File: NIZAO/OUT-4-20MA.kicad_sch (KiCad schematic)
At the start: 11 parts, among them Q1 NCE60P04R, U16 GP8302-TC50-EW

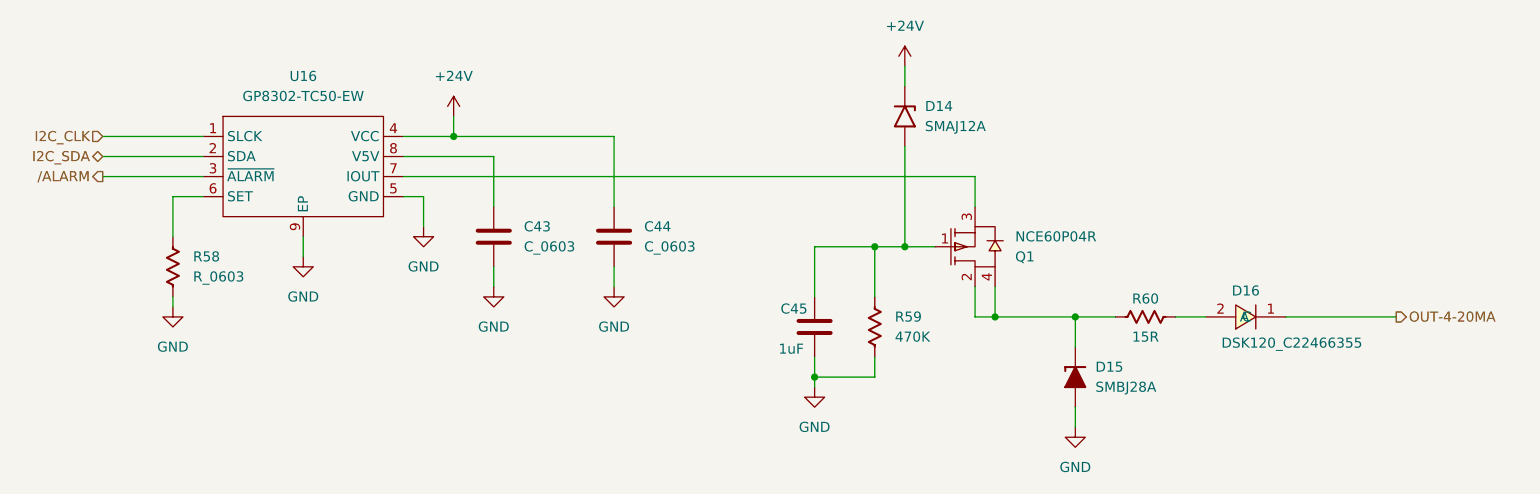
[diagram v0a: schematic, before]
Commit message: Colocandos los 3d de los componetes en la placa NIZAO
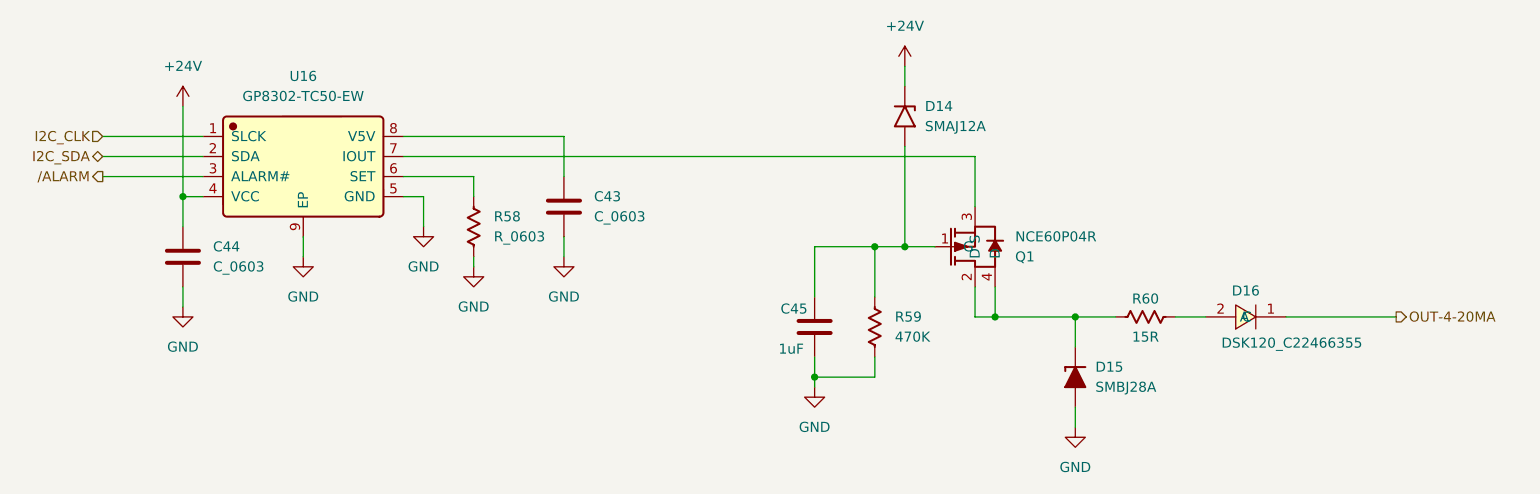
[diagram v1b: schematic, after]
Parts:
- Q1: footprint NCE NCE60P04R:SOT-223-3_L6.5-W3.4-P2.30-LS7.0-BR -> JLCImport:NCE60P04R; symbol EasyEDA:NCE60P04R -> JLCImport:NCE60P04R; LCSC (none) -> C502855; Manufacturer (none) -> Wuxi NCE Power Semiconductor; Manufacturer Part (none) -> NCE60P04R
- U16: footprint Guestgood GP8211S-TC50-EW:ESOP-8_L4.9-W3.9-P1.27-LS6.0-BL-EP -> JLCImport:GP8302-TC50-EW; symbol EasyEDA:GP8302-TC50-EW -> JLCImport:GP8302-TC50-EW; LCSC (none) -> C2856295; Manufacturer (none) -> Guestgood; Manufacturer Part (none) -> GP8302-TC50-EW
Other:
- moved on the sheet: C43, C44, R58
